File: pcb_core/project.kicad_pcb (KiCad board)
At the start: 2 copper layers, 212.3 x 91.7 mm, 143 parts, among them IC1 DRV8871DDA, IC10 DRV8871DDA, IC11 DRV8871DDA, IC12 DRV8871DDA, IC13 DRV8871DDA, IC14 DRV8871DDA, IC15 DRV8871DDA, IC16 DRV8871DDA, IC17 DRV8871DDA, IC18 DRV8871DDA, IC19 SX1509QBIULTRT, IC2 SX1509QBIULTRT, IC3 DRV8871DDA, IC4 TCA9548APWR, IC5 DRV8871DDA, IC6 DRV8871DDA, IC7 DRV8871DDA, IC8 DRV8871DDA, IC9 DRV8871DDA, J1 Conn_01x02, J10 1053131103, J11 1053131103, J12 1053131103, J13 1053131103, J14 1053131103, J15 1053131103, J16 1053131103, J17 1053131103, J18 1053131103, J19 Conn_02x02_Counter_Clockwise, J2 1725656, J20 PCBConnector, J21 PCBConnector, J22 PCBConnector, J23 PCBConnector, J25 PCBConnector, J27 PCBConnector, J3 1053131103, J4 1053131103, J5 1053131103, J6 1053131103, J7 1053131103, J8 1053131103, J9 1053131103, Q1 SI9945BDY-T1-GE3, U1 ESP32-S3-WROOM-2, U2 LTC4365TS8, U3 ESP32-DevKitC

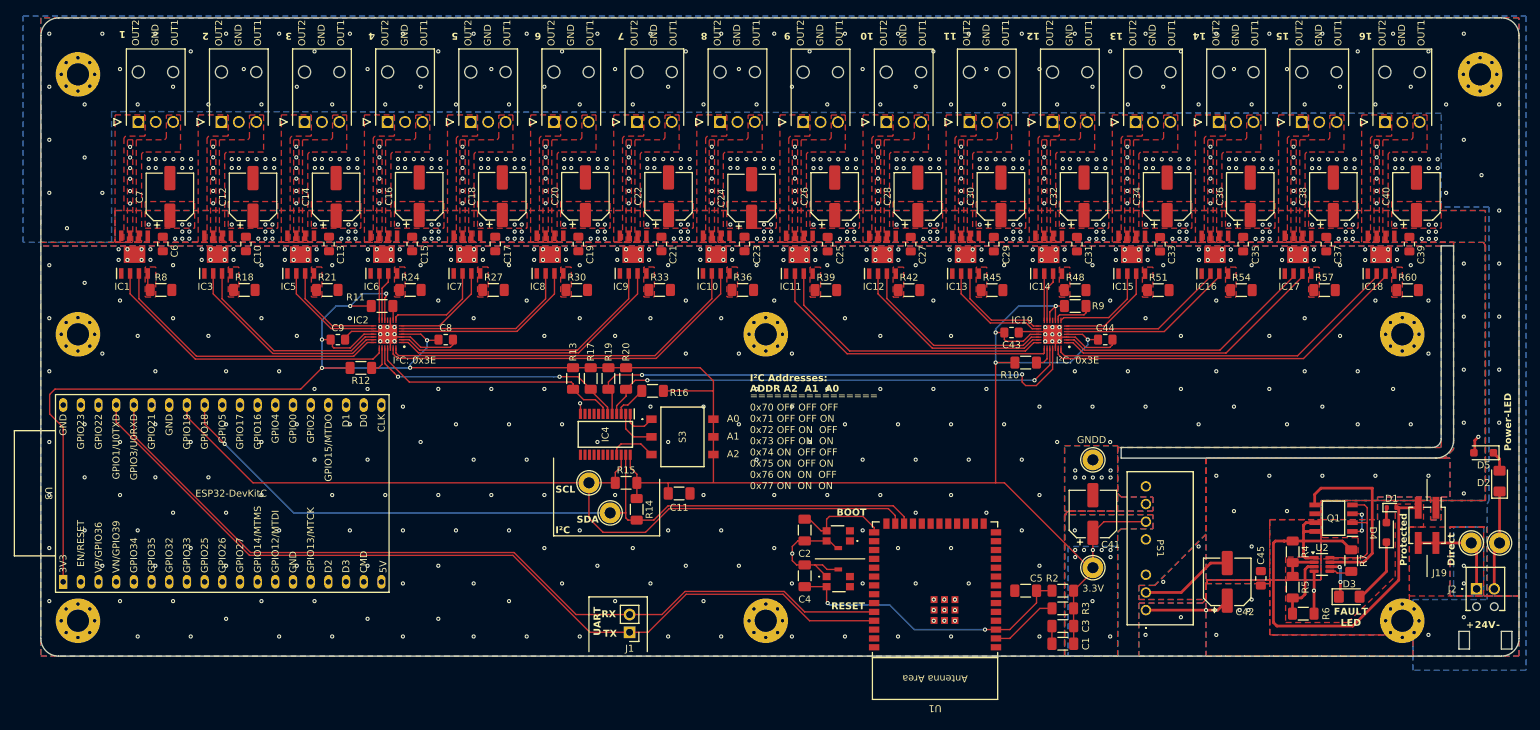
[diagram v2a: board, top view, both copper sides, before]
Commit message: Move location of power line led and set LCSC-IDs
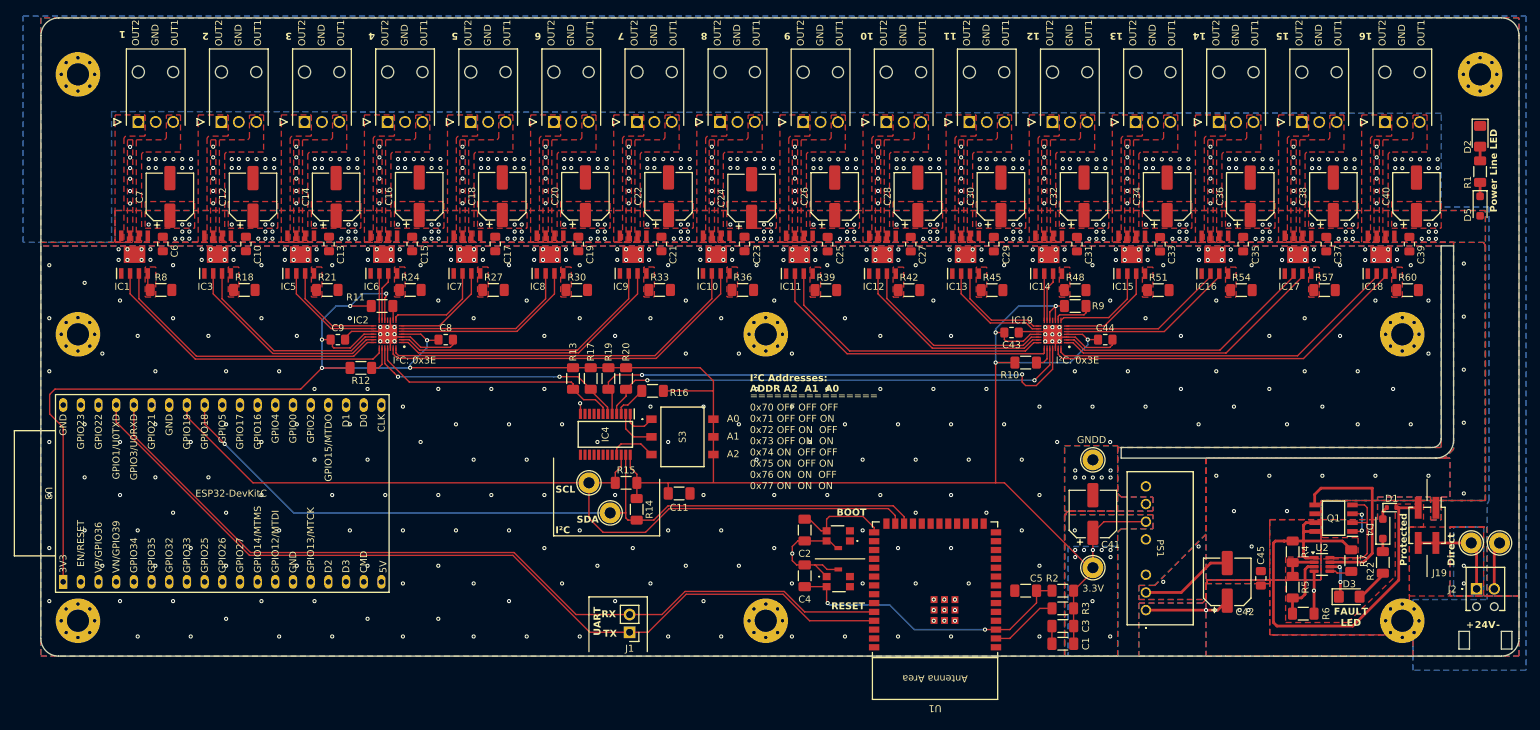
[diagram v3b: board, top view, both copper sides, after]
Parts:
- added R1: 1.1k, Resistor_SMD:R_1206_3216Metric_Pad1.30x1.75mm_HandSolder, F.Cu at (255.0, 63.0)
- added R22: 1.1k, Resistor_SMD:R_1206_3216Metric_Pad1.30x1.75mm_HandSolder, F.Cu at (241.0, 119.1)
- moved D2 49.6 mm to (255.0, 57.9), turned to -90 degrees
- moved D5 35.4 mm to (255.0, 67.9), turned to -90 degrees
- moved D4 0.72 mm to (241.0, 114.3)
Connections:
- D4 pad 1: Net-(D3-A) -> Net-(D4-K)
- D5 pad 1: Net-(D2-A) -> Net-(D5-K)
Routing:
- net GNDA: track 33.8 -> 26.4 mm, vias 362 -> 261
- net Net-(D3-A): track 9.57 -> 4.89 mm
- net PROD_24V: track 42.1 -> 39.6 mm, vias 144 -> 143
- net Net-(D5-K): track 0.00 -> 2.00 mm
- net Net-(D4-K): track 0.00 -> 1.88 mm
- net Net-(D2-A): track 2.94 -> 2.04 mm
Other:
- board text added: "Power Line LED"
- board text removed: "Power-LED"

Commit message: Correct variant setting for components
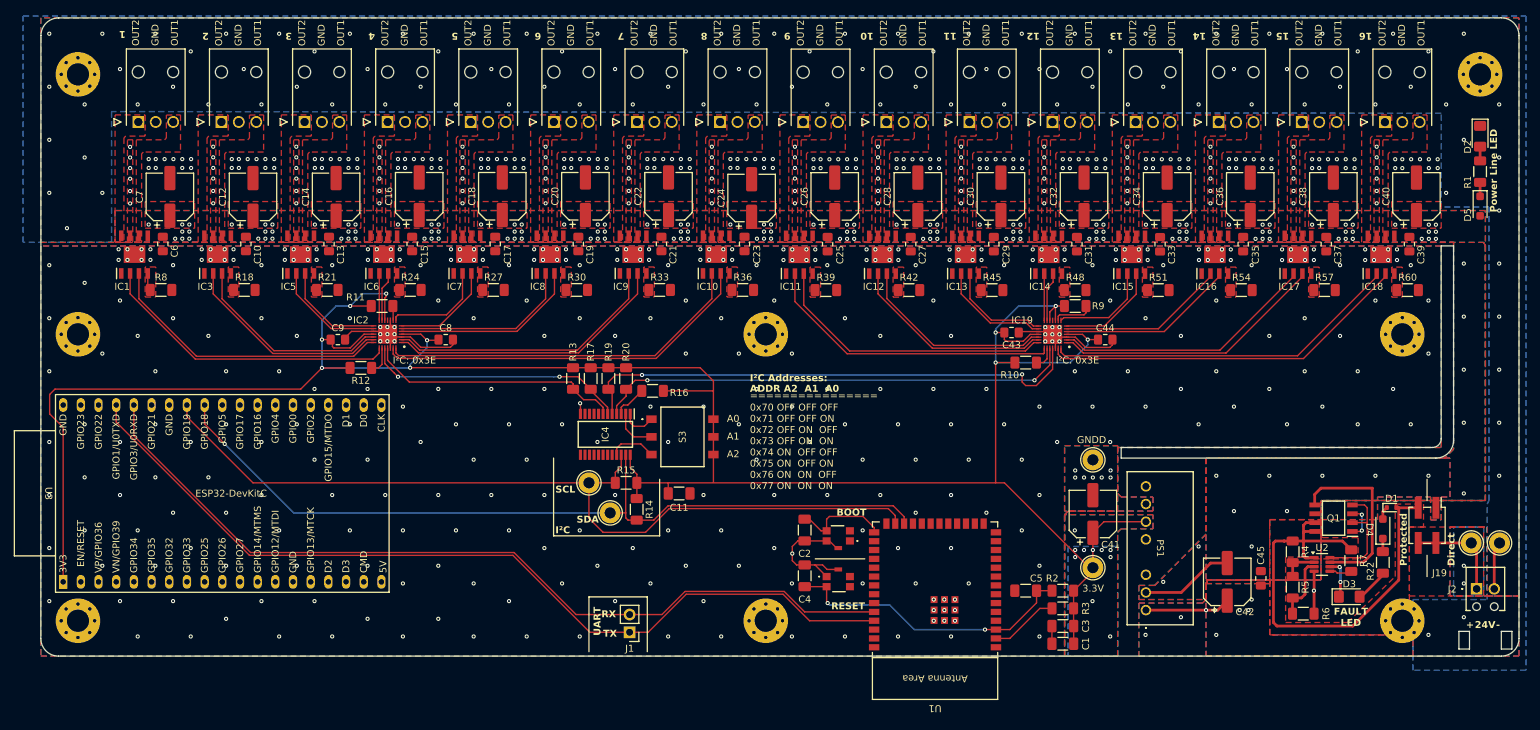
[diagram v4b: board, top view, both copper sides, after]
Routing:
- net GNDA: vias 261 -> 363

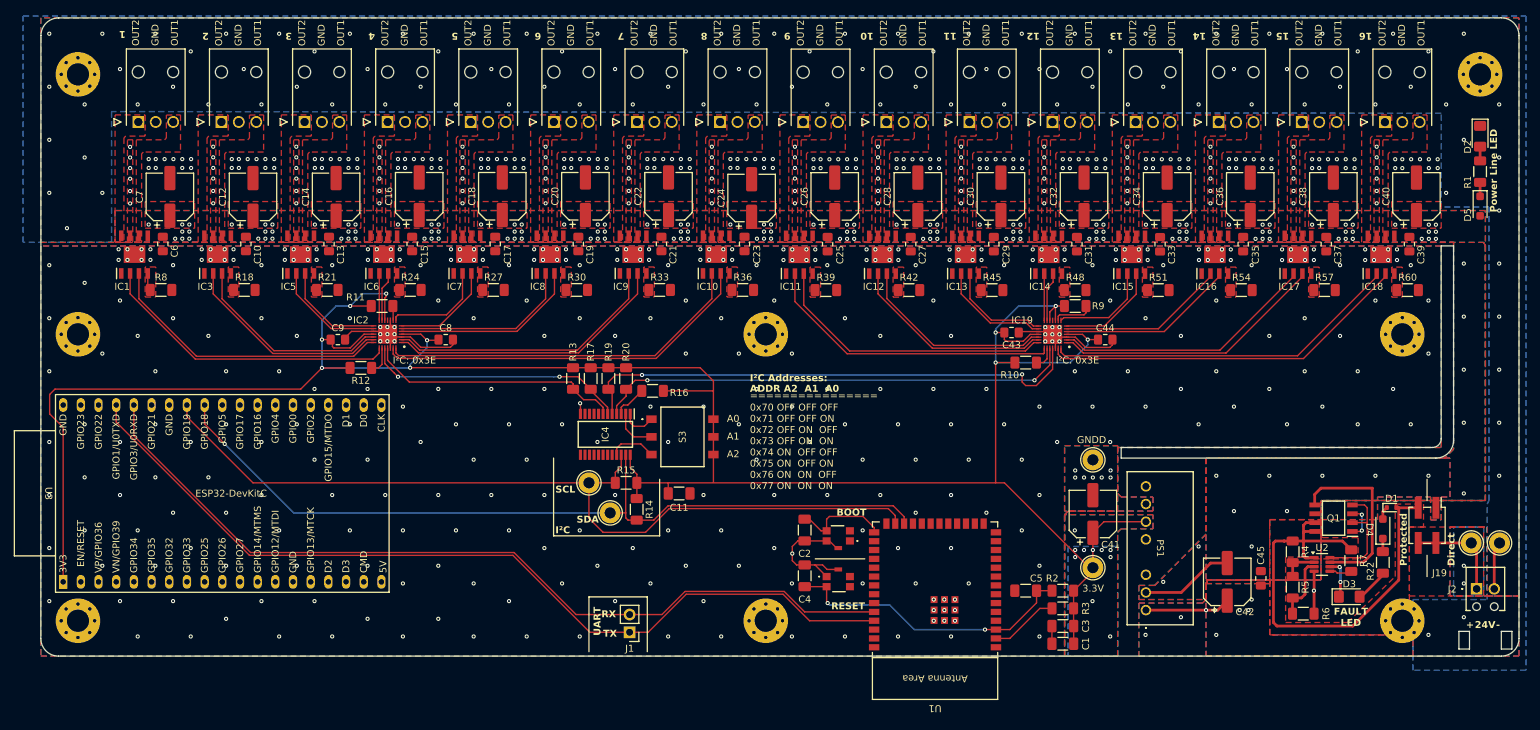
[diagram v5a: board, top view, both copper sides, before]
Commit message: Add LED for 3.3V power line
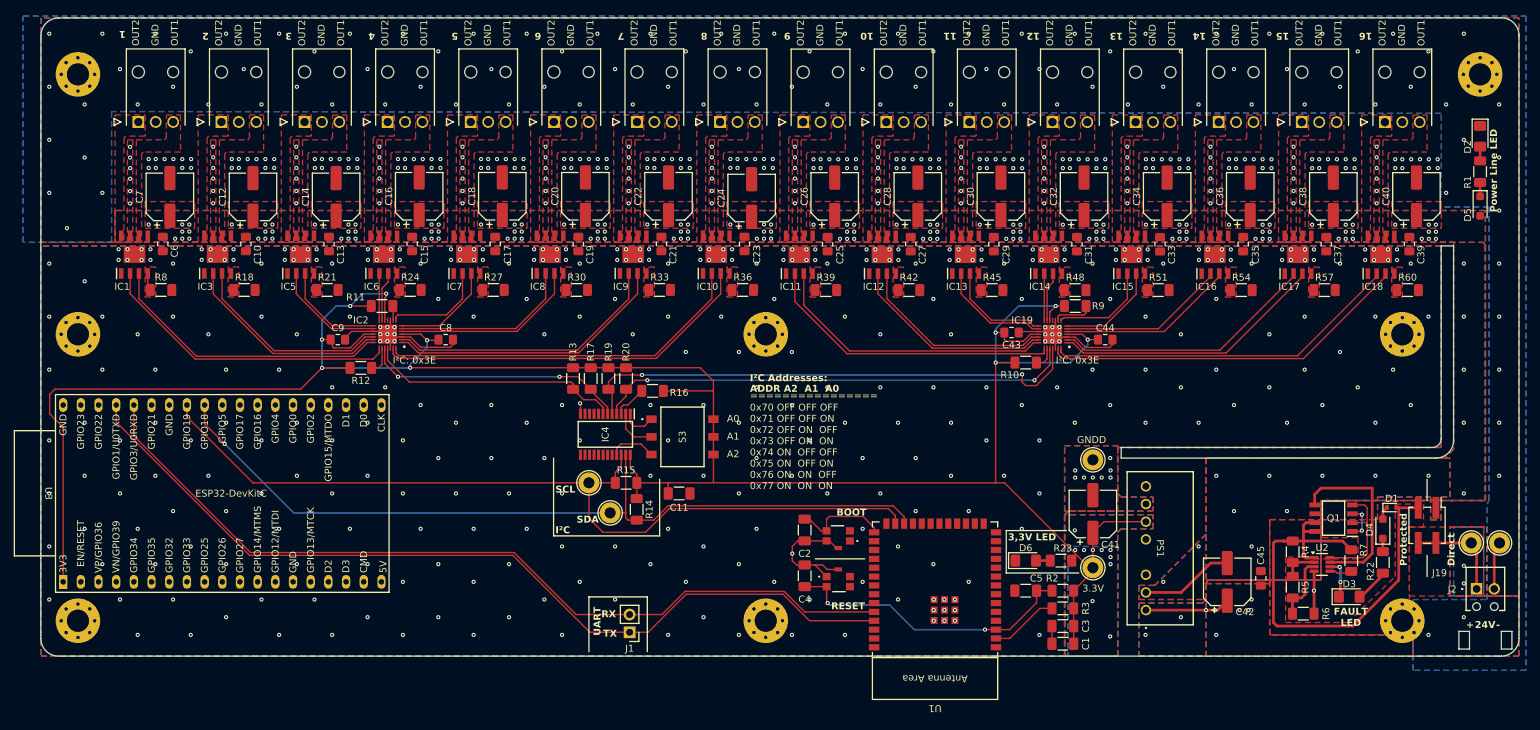
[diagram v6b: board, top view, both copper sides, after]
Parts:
- added D6: GREEN LED, LED_SMD:LED_1206_3216Metric_Pad1.42x1.75mm_HandSolder, F.Cu at (189.7, 118.9)
- added R23: 56, Resistor_SMD:R_1206_3216Metric_Pad1.30x1.75mm_HandSolder, F.Cu at (194.8, 118.9)
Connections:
- IC19 pad 10: VCC_3V3 -> GNDD
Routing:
- net GNDD: track 62.8 -> 64.9 mm, vias 370 -> 369
- net Net-(D6-A): track 0.00 -> 2.04 mm
- net VCC_3V3: track 367.5 -> 365.5 mm
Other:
- board text added: "3,3V LED"
